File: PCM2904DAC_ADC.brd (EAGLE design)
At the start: 85 x 56 mm, 27 parts, among them Q1 12MHz, X1 V+, D-, D+, GND, X2 1503_09, X3 1503_09

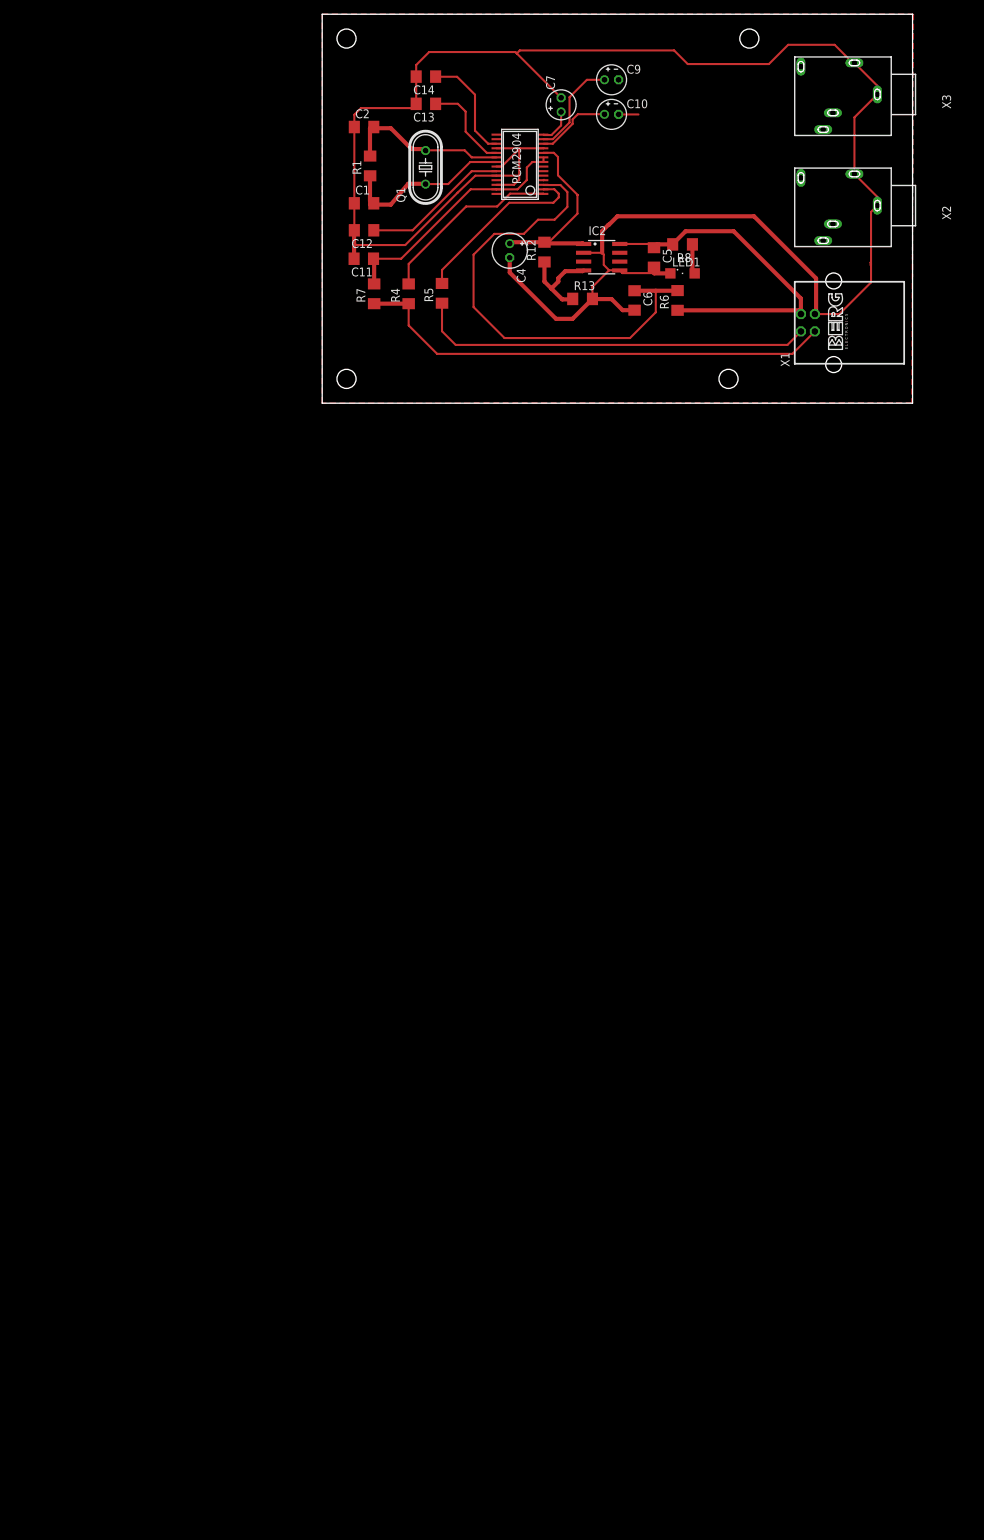
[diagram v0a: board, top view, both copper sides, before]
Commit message: Agregados etapas preamplificadoras...
... y cambiado el ordenamiento y routeo de pistas
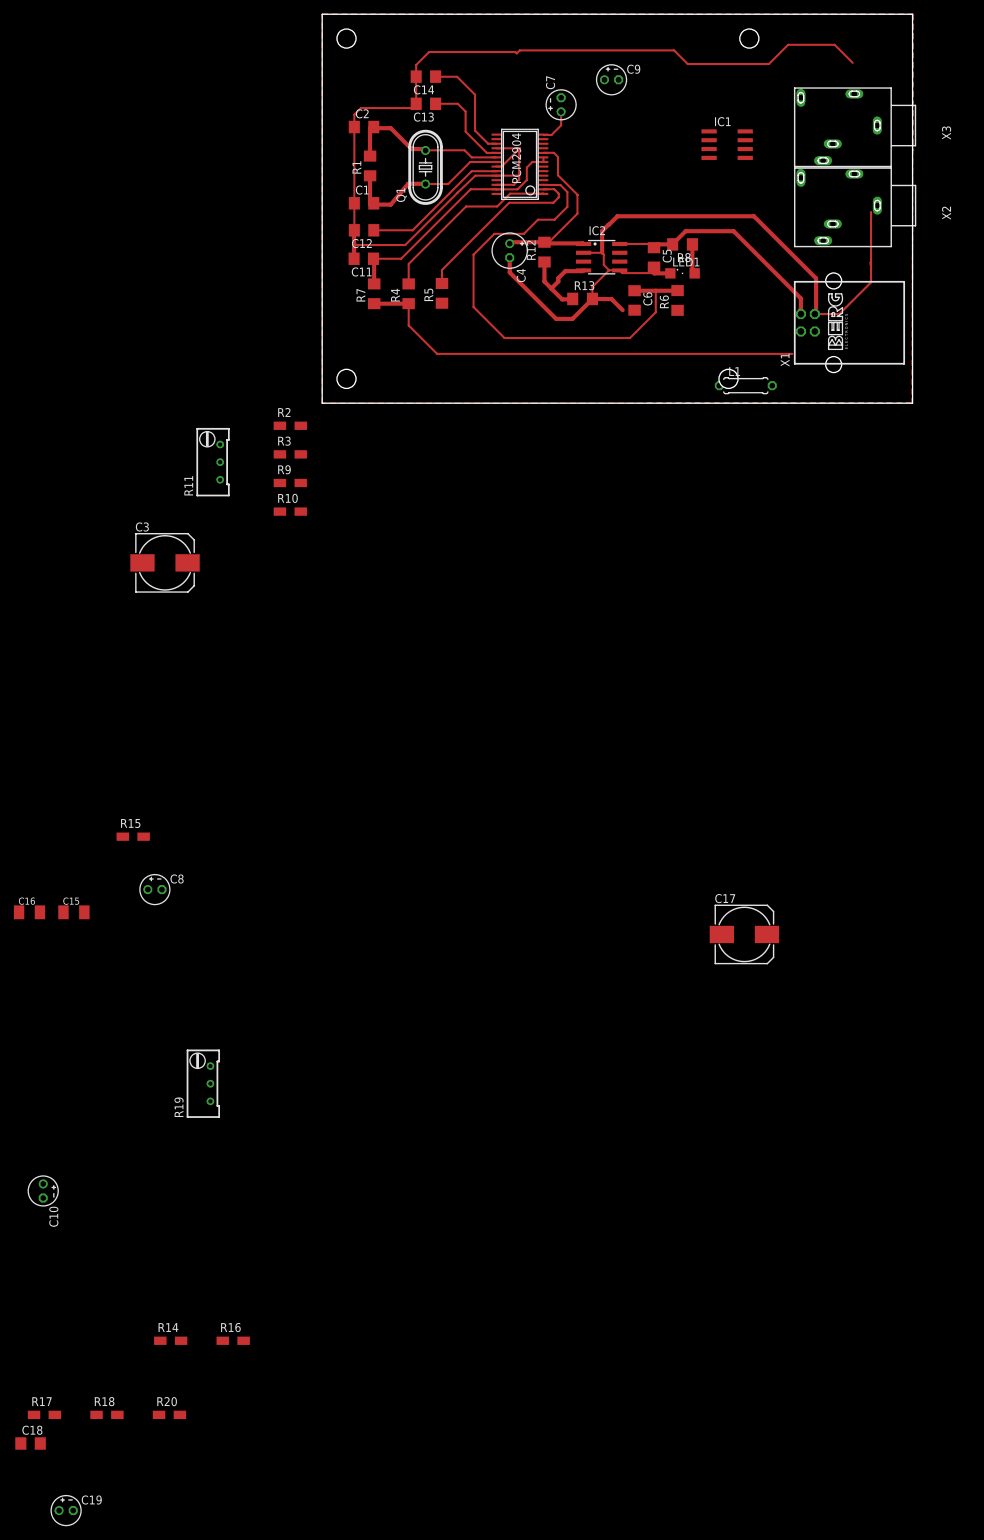
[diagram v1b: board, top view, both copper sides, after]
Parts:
- added C15, C16: (no value), rcl:C1206K
- added C17, C3: (no value), rcl:153CLV-0810
- added C18: 0.1u, rcl:C1206
- added C19, C8: 10u, rcl:E2-4
- added IC1: LM358D, linear:SO08
- added L1: (no value), rcl:0207/7
- added R10, R14, R15, R16, R17, R18, R2, R20, R3, R9: (no value), rcl:R1206W
- added R11, R19: (no value), rcl:RTRIM64W
- moved C10 175.3 mm to (-40.2, -113.4), turned to 270 degrees
- moved X3 4.47 mm to (82.0, 40.0)
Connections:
- net N$7 renamed D+
- net N$8 renamed D-
- removed net N$40: C4.+, IC2.1, PCM2904.10, R12.2
- new net +3V3: C4.+, IC2.1, R12.2
- new net +5V: C11.1, C16.1, C18.1, C19.+, C5.1, C8.+, IC1.8, IC2.8, L1.2, PCM2904.27, PCM2904.8, PCM2904.9, R14.2, R17.2, R2.2, R6.1, R7.2, R8.2, R9.2
- new net CH-L: C9.-, PCM2904.12
- new net CH-R: C10.-, PCM2904.13
- new net N$17: R10.1, R11.1
- new net N$18: C9.+, IC1.1, R11.2, R11.3
- new net N$19: IC1.3, R15.2, R9.1
- new net N$22: IC1.5, R17.1, R20.2
- new net N$5: C3.+, R2.1, X2.3
- new net N$7: C17.+, R14.1, X3.3
- new net N$8: C15.1, L1.1, X1.1
- net GND: now also C15.2, C16.2, C18.2, C19.-, C8.-, IC1.4, R15.1, R20.1; no longer PCM2904.11, X2.2, X3.2
- net N$10: now also IC1.6, R16.1, R18.2; no longer C10.+, PCM2904.12
- net N$12: now also R18.1, R19.1; no longer C11.1, PCM2904.27, PCM2904.8, PCM2904.9, R7.2
- net N$13: now also C3.-, R3.2; no longer C10.-, X2.3
- net N$14: now also C10.+, IC1.7, R19.2, R19.3; no longer C9.+, PCM2904.13
- net N$15: now also IC1.2, R10.2, R3.1; no longer C9.-, X3.3
- net N$9: now also C17.-, R16.2; no longer C5.1, IC2.8, R6.1, R8.2, X1.1
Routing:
- net +5V: track 0.00 -> 69.9 mm
- net D-: track 57.3 -> 0.00 mm
- net N$9: track 51.9 -> 0.00 mm
- net GND: track 295.7 -> 254.9 mm
- net N$12: track 35.6 -> 0.00 mm
- net N$40: track 29.0 -> 0.00 mm
- net +3V3: track 0.00 -> 29.0 mm
- net N$14: track 14.5 -> 0.00 mm
- net N$10: track 11.1 -> 0.00 mm
- net D+: track 69.6 -> 65.0 mm
- net N$13: track 2.87 -> 0.00 mm

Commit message: Commit adicional
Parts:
- C10, C19, C8, C9: device rcl:E2-4 -> rcl:153CLV-0505
- C17, C3: device rcl:153CLV-0810 -> rcl:153CLV-0505
- moved C19 223.6 mm to (57.6, 43.2), turned to 180 degrees
- moved C18 221.3 mm to (57.6, 47.8)
- moved R17 208.4 mm to (60.0, 37.1), turned to 90 degrees
- moved R18 208.1 mm to (36.8, 51.1)
- moved R14 202.4 mm to (79.3, 40.4)
- moved R20 196.3 mm to (56.7, 34.1), turned to 90 degrees
- moved R16 191.1 mm to (66.3, 38.9), turned to 90 degrees
- moved C10 168.5 mm to (26.6, 41.3), turned to 90 degrees
- moved R19 157.2 mm to (29.2, 52.2), turned to 90 degrees
- moved C16 138.4 mm to (63.5, 16.1), turned to 270 degrees
- moved C15 130.5 mm to (63.5, 11.5), turned to 90 degrees
- moved R15 119.8 mm to (41.9, 35.4), turned to 90 degrees
- moved C8 118.5 mm to (58.1, 15.4), turned to 90 degrees
- moved C17 117.4 mm to (71.9, 40.4)
- moved C3 105.0 mm to (71.8, 22.9)
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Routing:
- net GND: track 254.9 -> 24.0 mm
- net +5V: track 69.9 -> 173.8 mm
- net D-: track 0.00 -> 80.2 mm
- net N$14: track 0.00 -> 50.0 mm
- net N$15: track 0.00 -> 43.2 mm
- net N$10: track 0.00 -> 38.1 mm
- net D+: track 65.0 -> 95.1 mm
- net N$18: track 0.00 -> 27.2 mm
- net +3V3: track 29.0 -> 6.72 mm
- net N$4: track 26.5 -> 8.83 mm
- net N$6: track 26.1 -> 12.0 mm
- net N$24: track 21.2 -> 7.56 mm
- net N$2: track 24.7 -> 11.5 mm
- net CH-L: track 0.00 -> 11.8 mm
- net N$1: track 25.8 -> 14.2 mm
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
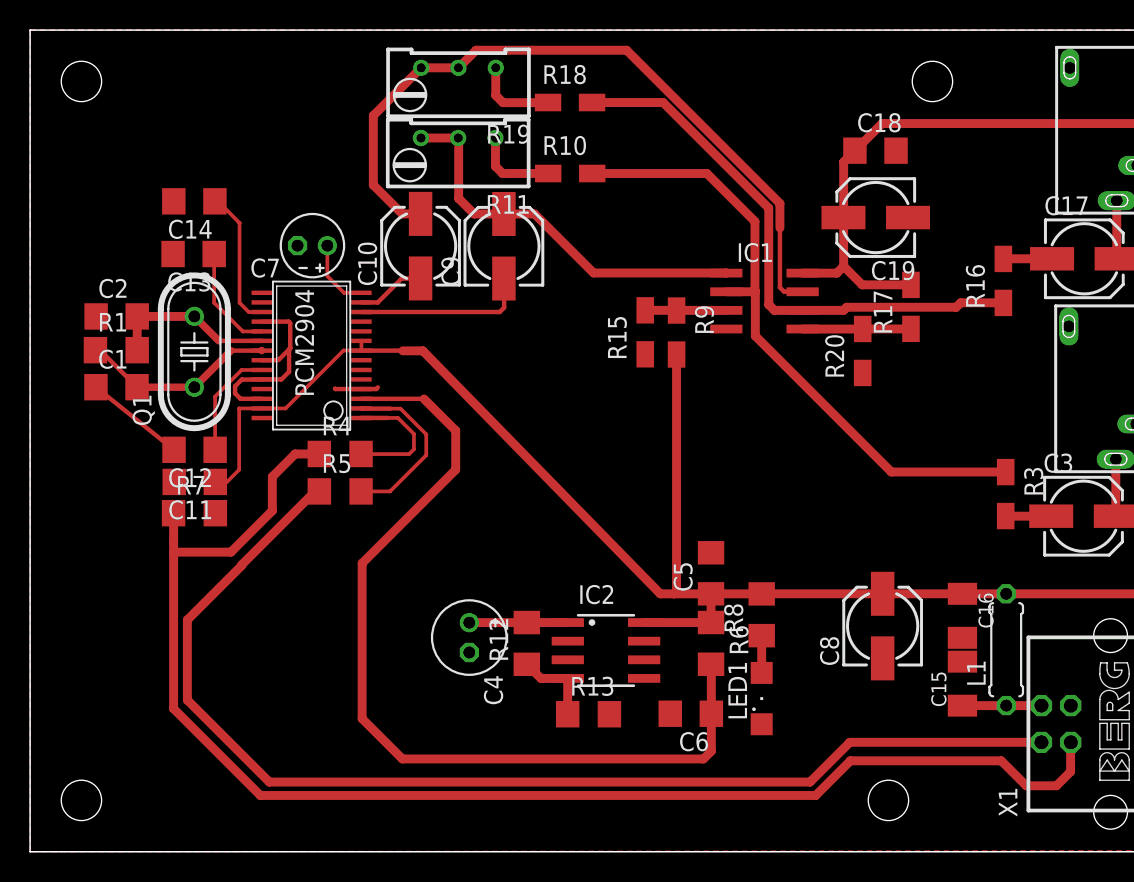
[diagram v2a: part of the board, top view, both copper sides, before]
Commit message: movi un poco las cosas de lugar, para que el plano de masa no se corte
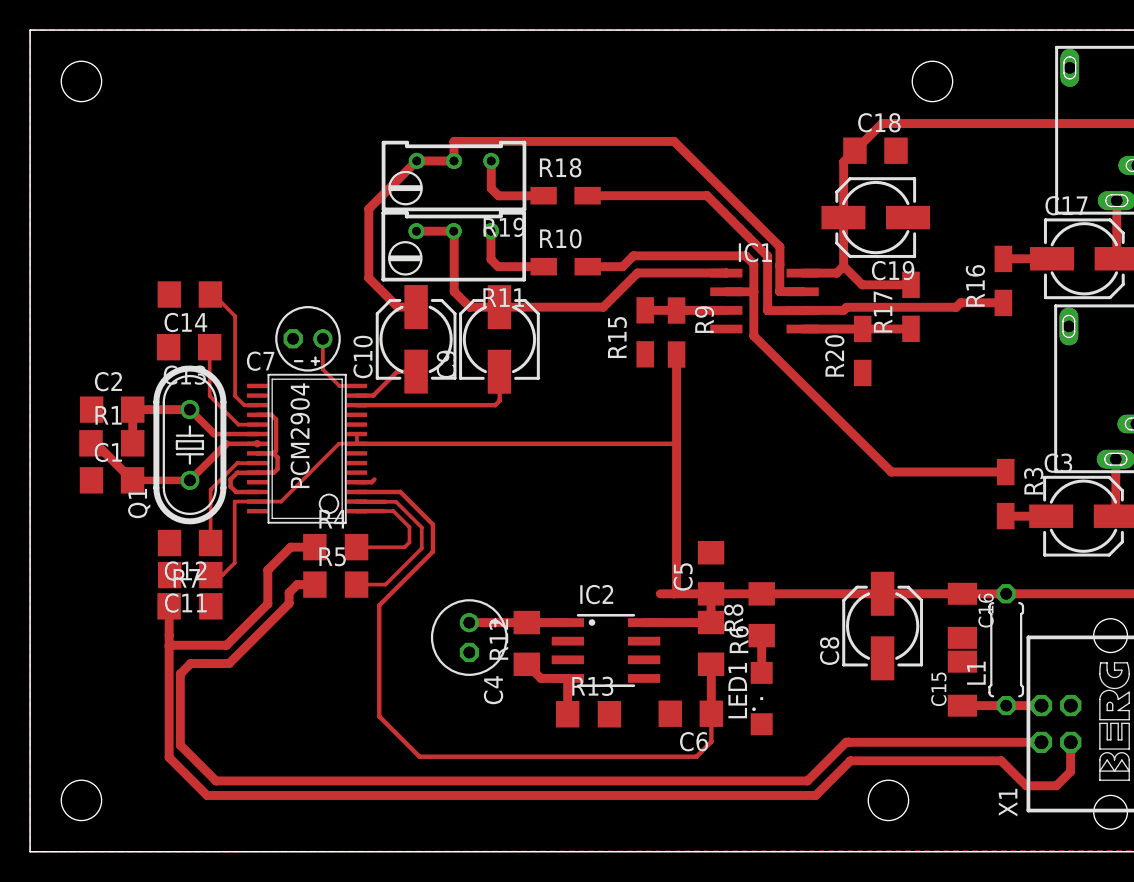
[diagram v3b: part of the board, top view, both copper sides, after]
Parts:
- moved C1 6.36 mm to (5.58, 25.3)
- moved C10 6.36 mm to (26.3, 34.9)
- moved C11 6.36 mm to (10.9, 18.9)
- moved C12 6.36 mm to (10.9, 21.0)
- moved C13 6.36 mm to (10.8, 34.4)
- moved C2 6.36 mm to (5.60, 30.1)
- moved C9 6.36 mm to (32.0, 34.9)
- moved Q1 6.36 mm to (10.9, 27.7)
- moved R10 6.36 mm to (36.5, 39.9)
- moved R18 6.36 mm to (36.5, 44.7)
- moved R7 6.36 mm to (10.9, 16.7)
- moved C7 6.36 mm to (18.9, 35.0)
- moved PCM2904 6.36 mm to (19.4, 27.2)
- moved R1 6.36 mm to (5.57, 27.8)
- moved R4 6.36 mm to (20.8, 20.8)
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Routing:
- net GND: track 24.0 -> 13.3 mm
- net N$11: track 60.7 -> 50.2 mm
- net +5V: track 173.8 -> 168.3 mm
- net D+: track 95.1 -> 91.1 mm
- net N$10: track 38.1 -> 34.1 mm
- net N$15: track 43.2 -> 39.6 mm
- net N$14: track 50.0 -> 47.1 mm
- net D-: track 80.2 -> 78.5 mm
- net N$18: track 27.2 -> 26.6 mm

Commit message: Mas cosas
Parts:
- C4: device rcl:E2-5 -> rcl:153CLV-0505
- C7: device rcl:E2-4 -> rcl:153CLV-0505
- moved R5 3.58 mm to (18.4, 15.6)
- moved R4 2.99 mm to (18.4, 19.0)
- moved C11 1.85 mm to (9.27, 18.0)
- moved R2 1.84 mm to (79.4, 22.6), turned to 0 degrees
- moved C13 1.79 mm to (9.27, 35.2)
- moved C12 1.74 mm to (9.27, 20.5)
- moved C14 1.65 mm to (9.27, 37.7)
- moved Q1 1.65 mm to (9.27, 27.5)
- moved R7 1.65 mm to (12.1, 15.6), turned to 180 degrees
- moved C2 1.59 mm to (4.04, 29.9)
- moved R1 1.59 mm to (4.04, 27.4)
- moved C1 1.57 mm to (4.04, 25.0)
- moved C4 1.47 mm to (29.2, 13.3), turned to 90 degrees
- moved C7 1.24 mm to (18.4, 36.1)
- moved PCM2904 0.48 mm to (18.9, 27.2)
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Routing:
- net D-: track 78.5 -> 59.1 mm
- net D+: track 91.1 -> 72.3 mm
- net +5V: track 168.3 -> 173.2 mm
- net N$11: track 50.2 -> 46.3 mm
- net N$16: track 4.87 -> 8.53 mm
- net N$6: track 12.0 -> 15.4 mm
- net N$4: track 8.83 -> 11.7 mm
- net N$1: track 13.8 -> 15.8 mm
- net N$2: track 11.5 -> 13.1 mm
- net GND: track 13.3 -> 14.8 mm
- net N$15: track 39.6 -> 41.1 mm
- net N$24: track 7.56 -> 8.99 mm
- net N$21: track 7.38 -> 8.71 mm
- net N$20: track 9.51 -> 10.5 mm
- net +3V3: track 6.72 -> 7.44 mm
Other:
- outline, holes or cut-outs redrawn
- board text added: "JONICA 2017"
- board text added: "Marcuzzi Moya Soria"

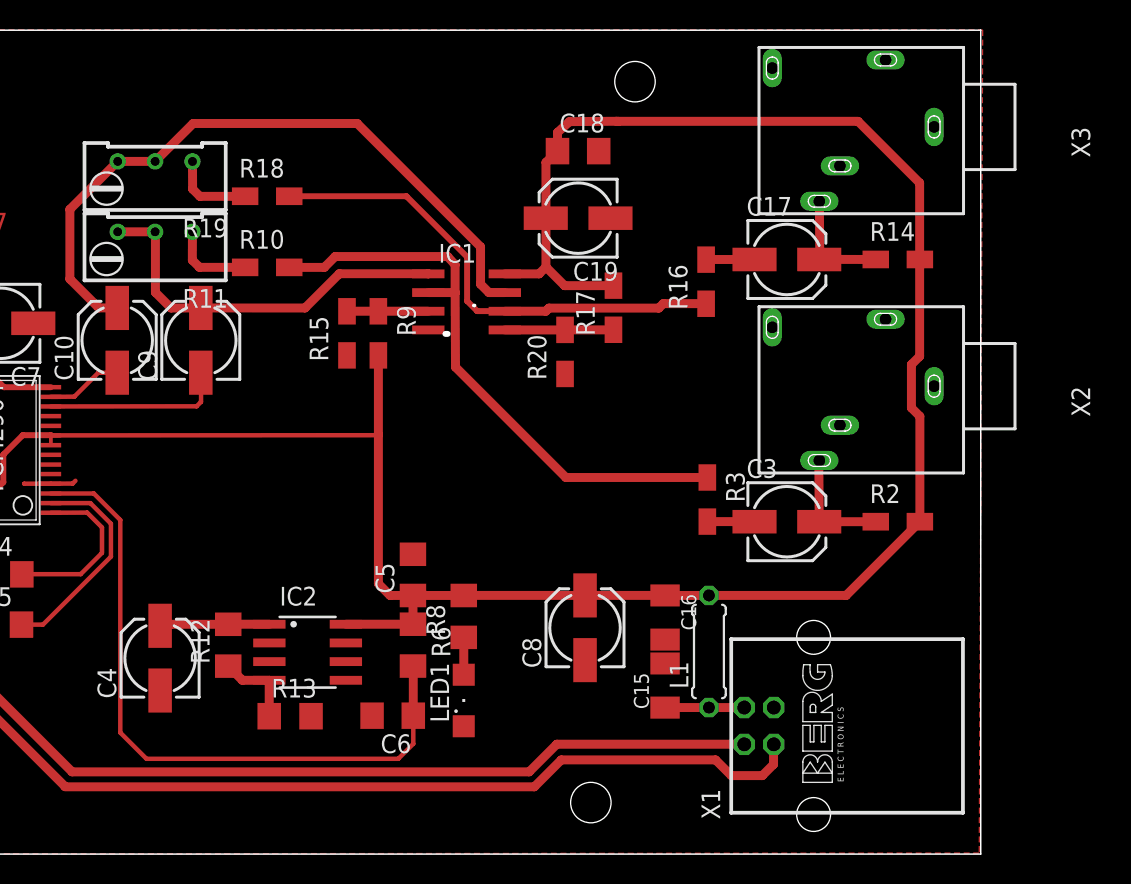
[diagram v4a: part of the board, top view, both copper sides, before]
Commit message: cambiado tamaño del led, fichas stereo, y otras cosas sueltas
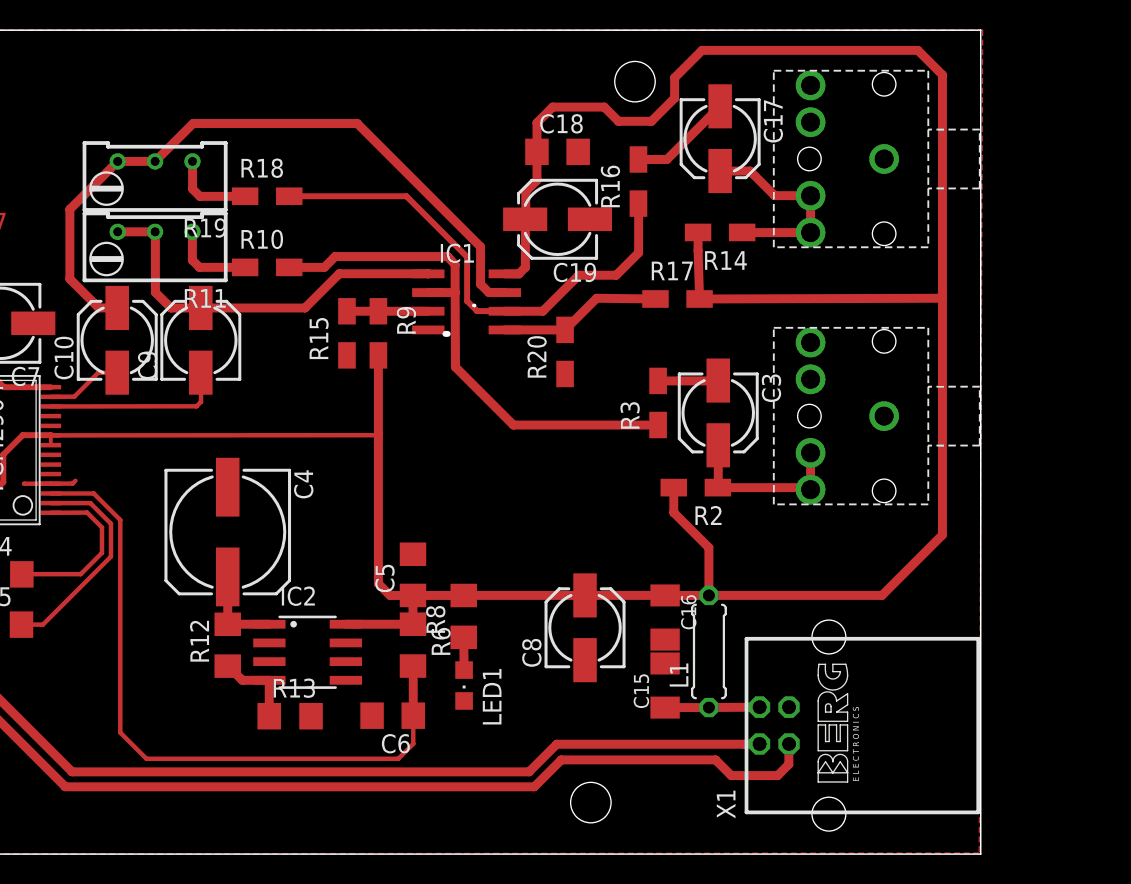
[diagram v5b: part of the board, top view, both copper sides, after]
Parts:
- removed X2, X3: 1503_09, con-lumberg:1503_09
- added U$1, U$8: 1/8STEREO, bleep t2:1/8STEREO
- C4: device rcl:153CLV-0505 -> rcl:153CLV-0807
- LED1: device led:SML1206 -> led:CHIPLED_0805
- moved R2 13.9 mm to (65.6, 24.9), turned to 180 degrees
- moved R14 12.2 mm to (67.3, 42.3), turned to 180 degrees
- moved C4 9.73 mm to (33.8, 21.9), turned to 270 degrees
- moved C17 9.38 mm to (67.3, 48.6), turned to 270 degrees
- moved C3 8.74 mm to (67.2, 30.0), turned to 270 degrees
- moved R16 8.21 mm to (61.7, 45.7)
- moved R3 7.37 mm to (63.1, 30.7), turned to 90 degrees
- moved R17 4.39 mm to (64.4, 37.7), turned to 0 degrees
- moved C19 1.40 mm to (56.2, 43.1)
- moved C18 1.40 mm to (56.2, 47.7)
- moved X1 1.04 mm to (74.7, 8.74)
- moved LED1 1.02 mm to (49.9, 11.5), turned to 180 degrees
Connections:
- net GND: now also U$1.P$1, U$8.P$1; no longer X2.1, X3.1
- net N$5: now also U$8.P$4, U$8.P$5; no longer X2.3
- net N$7: now also U$1.P$4, U$1.P$5; no longer X3.3
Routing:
- net +5V: track 173.2 -> 210.9 mm
- net N$7: track 7.88 -> 14.0 mm
- net N$15: track 41.1 -> 36.0 mm
- net N$9: track 3.29 -> 7.05 mm
- net N$22: track 7.53 -> 11.3 mm
- net N$5: track 8.04 -> 11.7 mm
- net N$8: track 5.40 -> 7.47 mm
- net +3V3: track 7.44 -> 6.05 mm
- net D+: track 72.3 -> 73.3 mm
- net D-: track 59.1 -> 60.1 mm
- net N$13: track 3.21 -> 4.10 mm
